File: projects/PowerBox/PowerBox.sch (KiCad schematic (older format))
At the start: 38 parts, among them CON1 USB-MICRO, CON2 USB-A-Jack, IC1 OPAMP-DUALU, P1 CONN_2, P2 CONN_2, P3 CONN_1, P4 CONN_1, P5 CONN_1, P6 CONN_1, U1 74HC595, U2 74HC595

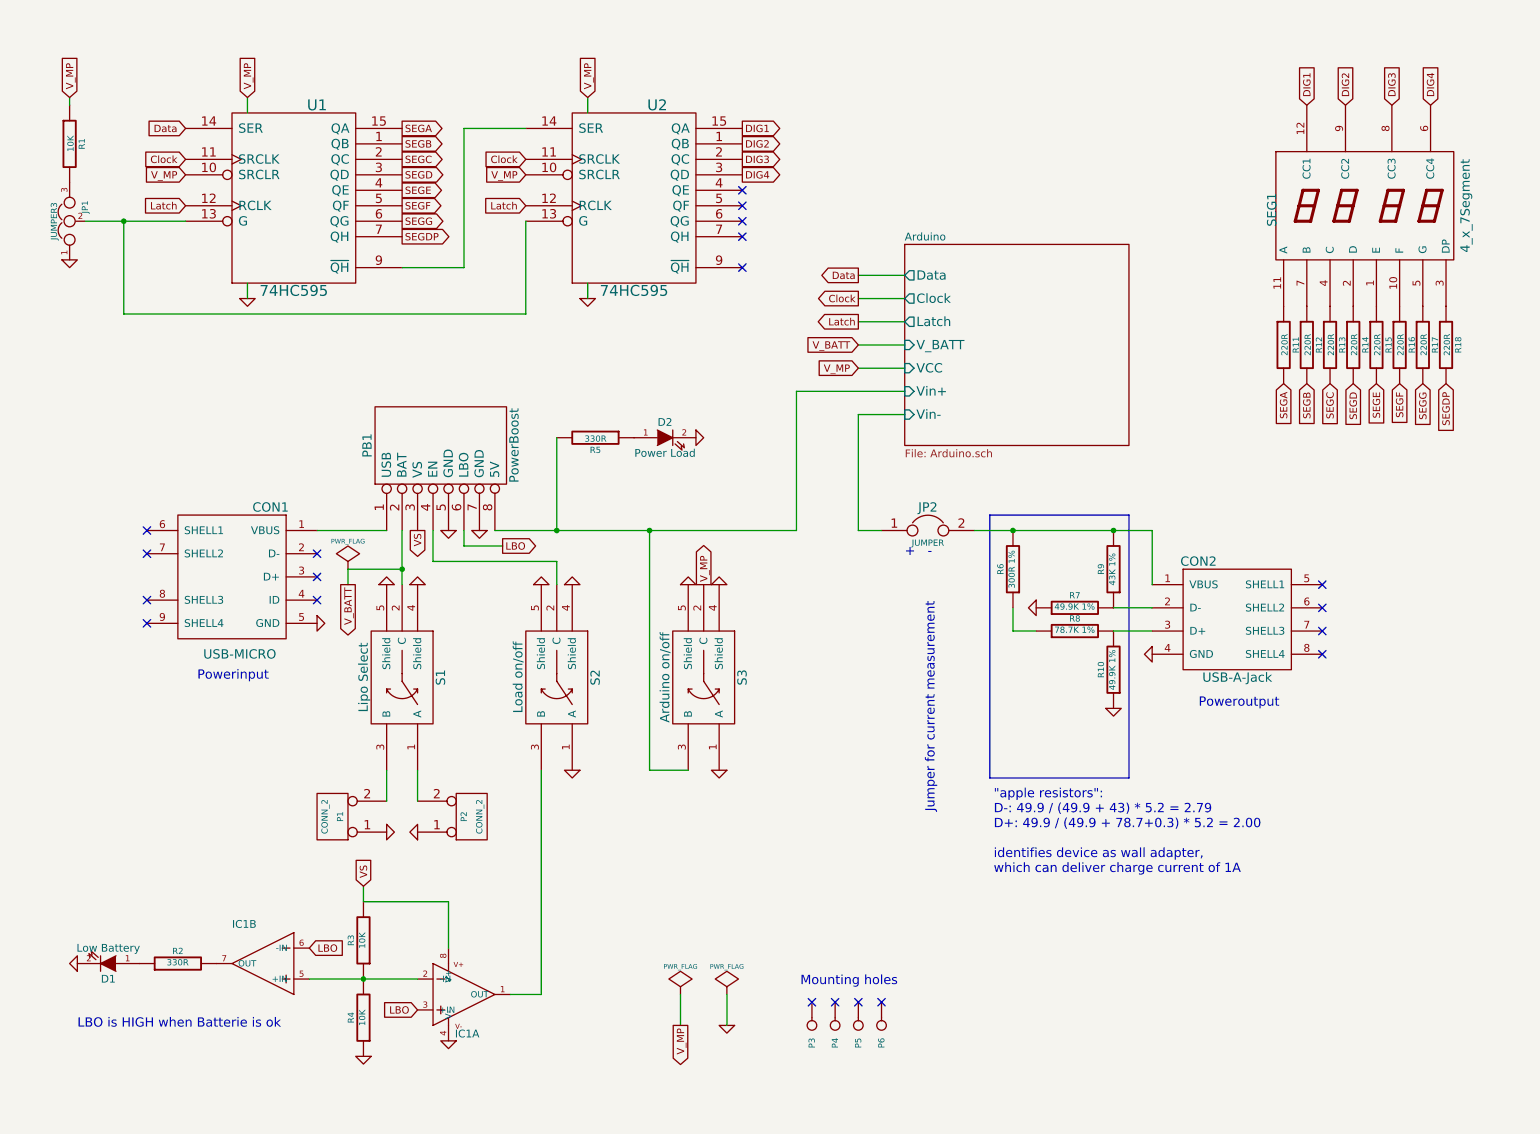
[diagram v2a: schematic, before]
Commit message: protection parts added
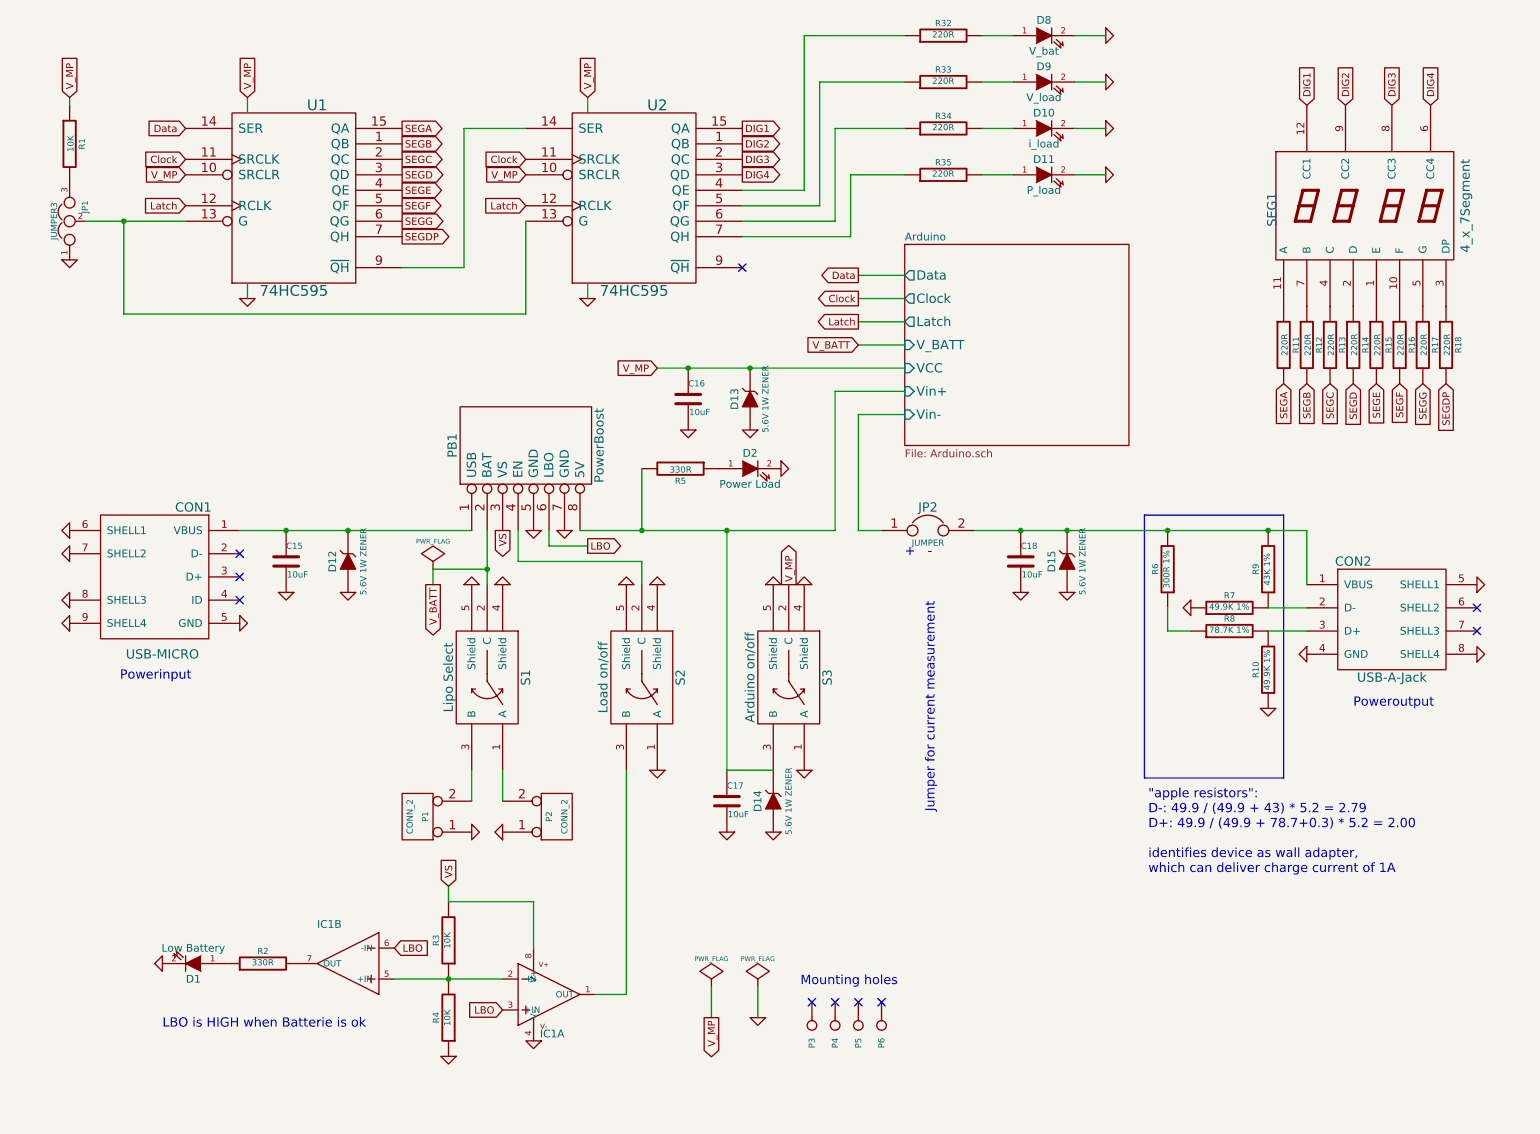
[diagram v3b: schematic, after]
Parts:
- added C15, C16, C17, C18: 10uF, frep:C0805, symbol C
- added D10: i_load, frep:LED-0805, symbol LED
- added D11: P_load, frep:LED-0805, symbol LED
- added D12, D13, D14, D15: 5.6V 1W ZENER, symbol ZENER
- added D8: V_bat, frep:LED-0805, symbol LED
- added D9: V_load, frep:LED-0805, symbol LED
- added R32, R33, R34, R35: 220R, frep:R0805, symbol R
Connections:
- net Arduino/Vin+: now also C17.1, D14.2 (K)
- net GND: now also CON1.6 (SHELL1), CON1.7 (SHELL2), CON1.8 (SHELL3), CON1.9 (SHELL4), CON2.5 (SHELL1), CON2.8 (SHELL4), C15.2, C16.2, C17.2, C18.2, D10.2 (K), D11.2 (K), D12.1 (A), D13.1 (A), D14.1 (A), D15.1 (A), D8.2 (K), D9.2 (K)
- net VCC: now also C16.1, D13.2 (K)
- net at CON1.1 (VBUS), PB1.1 (USB): now also C15.1, D12.2 (K)
- net at CON2.1 (VBUS), JP2.2, R6.2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: now also C18.1, D15.2 (K)
- net at U2.4 (QE): now also R32.1
- net at U2.5 (QF): now also R33.1
- net at U2.6 (QG): now also R34.1
- net at U2.7 (QH): now also R35.1
- new net: D11.1 (A), R35.2
- new net: D10.1 (A), R34.2
- new net: D9.1 (A), R33.2
- new net: D8.1 (A), R32.2
- no-connect marks 20 -> 10
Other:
- moved on the sheet: CON1, D1, D2, IC1A, IC1B, P1, P2, PB1, R10, R2, R3, R4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

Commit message: Switches changed
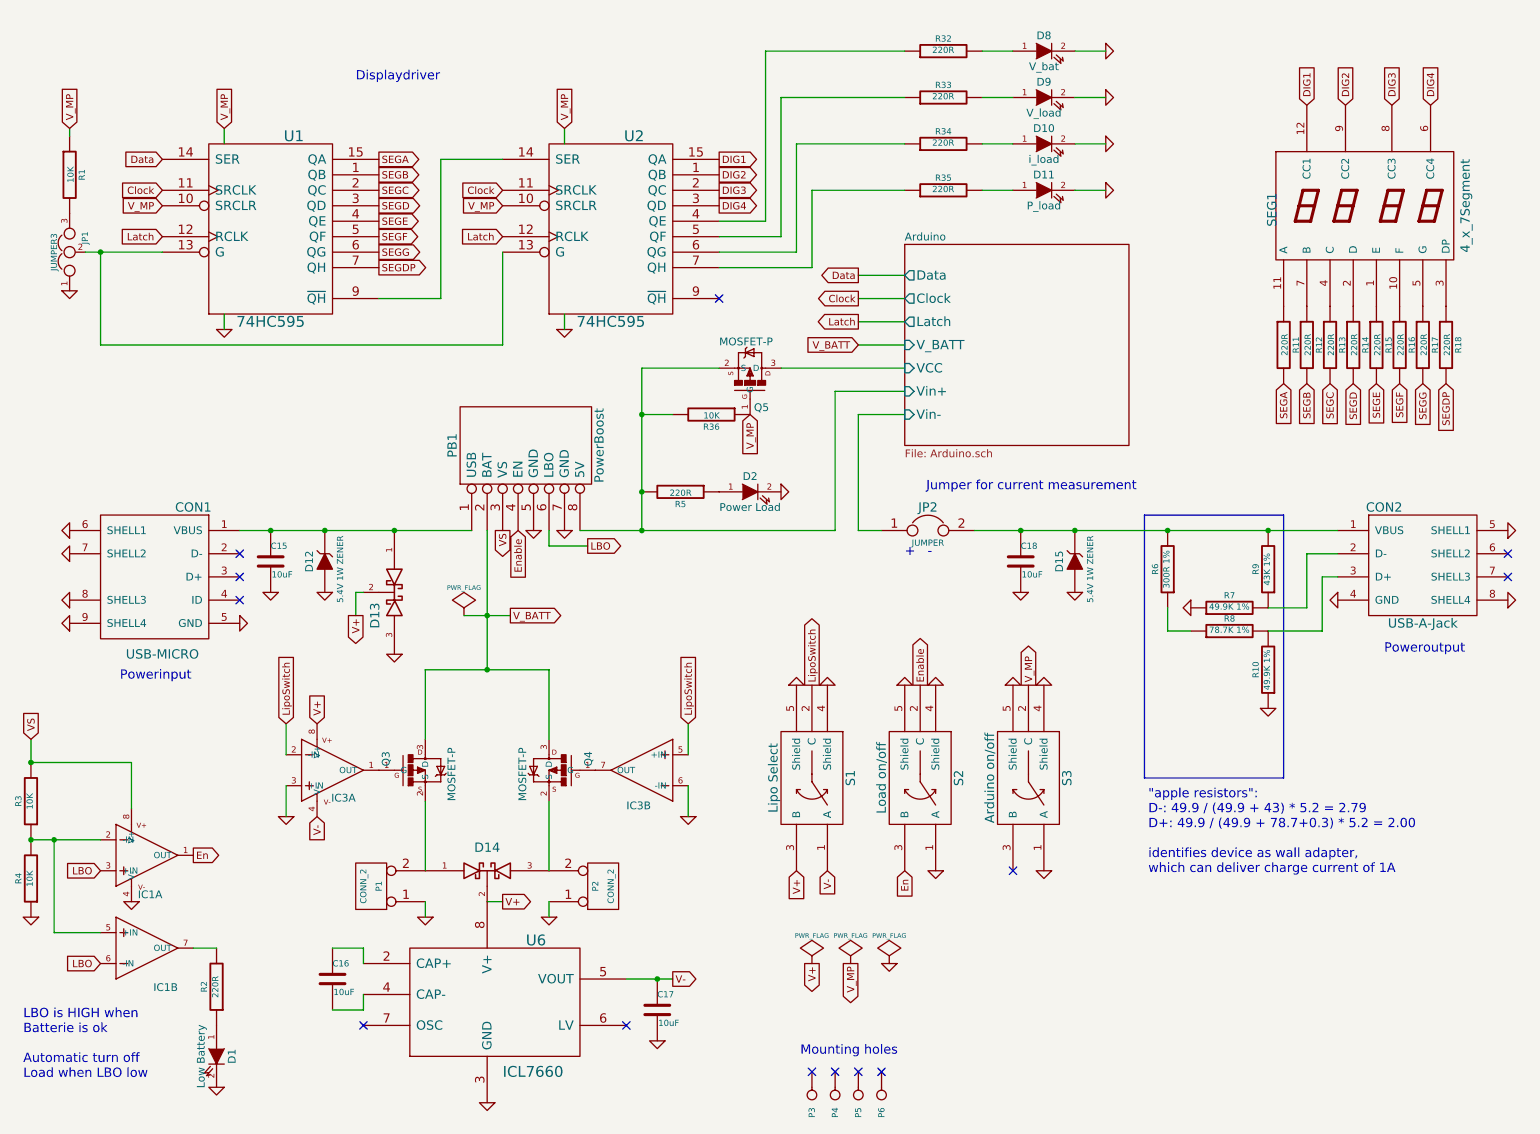
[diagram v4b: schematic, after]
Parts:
- removed D13, D14: 5.6V 1W ZENER, symbol ZENER
- added D13, D14: DOUBLE_SCH_KCOM, symbol DOUBLE_SCH_KCOM
- added IC3: OPAMP-DUALU, SparkFun-SO08, symbol OPAMP-DUALU
- added Q3, Q4, Q5: MOSFET-P, symbol MOSFET-P
- added R36: 10K, frep:R0805, symbol R
- added U6: ICL7660, symbol ICL7660
- D12, D15: value 5.6V 1W ZENER -> 5.4V 1W ZENER
- R2, R5: value 330R -> 220R
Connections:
- net Arduino/Vin+: now also Q5.2 (S), R36.2; no longer C17.1, S3.3 (B)
- net GND: now also D13.3 (cathode), IC3.3 (+IN), IC3.6 (-IN), U6.3 (GND); no longer C16.2
- net VCC: now also Q5.1 (G), R36.1; no longer C16.1
- net V_BATT: now also Q3.3 (D), Q4.3 (D); no longer S1.2 (C)
- net at C15.1, CON1.1 (VBUS), D12.2 (K)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: now also D13.1 (Anode)
- net at P2.2 (PM): now also D14.3 (cathode), Q4.2 (S); no longer S1.1 (A)
- net at P1.2 (PM): now also D14.1 (Anode), Q3.2 (S); no longer S1.3 (B)
- net Enable: now reaches PB1.4 (EN), S2.2 (C)
- net En: now reaches IC1.1 (OUT), S2.3 (B)
- new net: IC3.1 (OUT), Q3.1 (G)
- new net: IC3.7 (OUT), Q4.1 (G)
- new net: C16.1, U6.2 (CAP+)
- new net: C16.2, U6.4 (CAP-)
- new net Arduino/VCC: Q5.3 (D)
- new net LipoSwitch: IC3.2 (-IN), IC3.5 (+IN), S1.2 (C)
- new net V+: D13.2 (AK), D14.2 (AK), IC3.8 (V+), S1.3 (B), U6.8 (V+)
- new net V-: C17.1, IC3.4 (V-), S1.1 (A), U6.5 (VOUT)
- no-connect marks 10 -> 13
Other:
- note added: "Displaydriver"
- note added: "LBO is HIGH when \nBatterie is ok\n\nAutomatic turn off\nLoad when LBO low"
- note removed: "LBO is HIGH when Batterie is ok"
- moved on the sheet: C15, CON2, D1, D10, D11, D12, D15, D2, D8, D9, IC1A, IC1B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

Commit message: part informations added
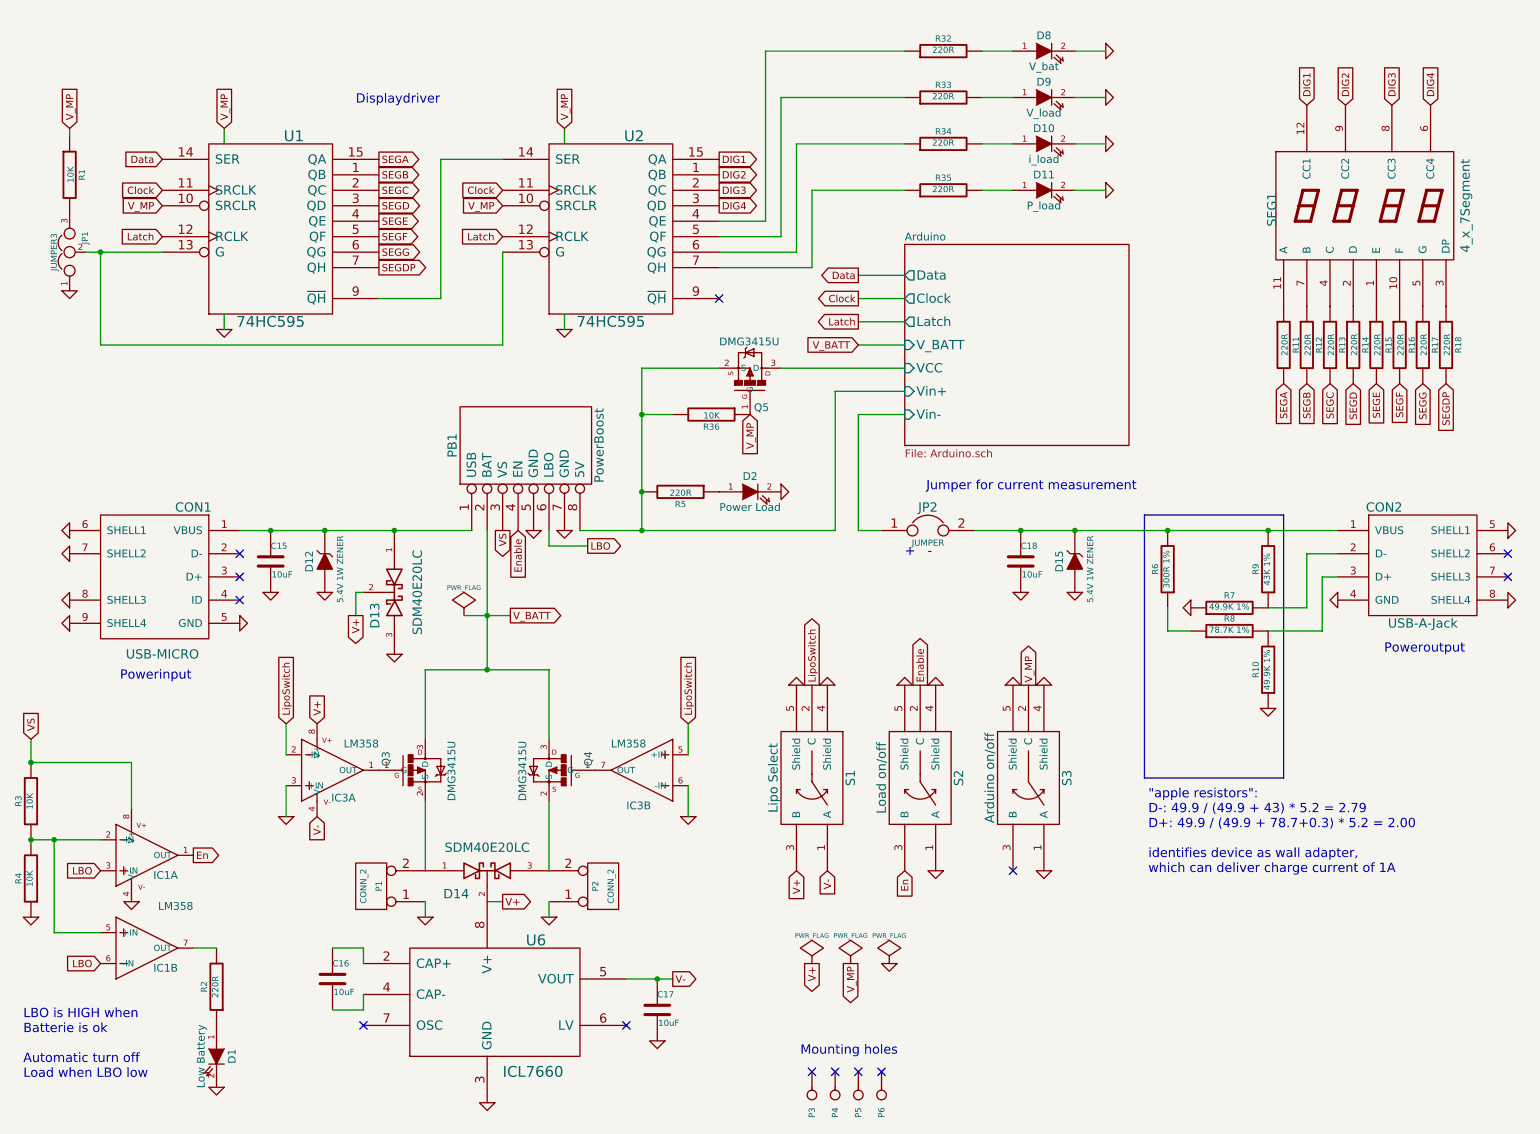
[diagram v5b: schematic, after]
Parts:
- D13, D14: value DOUBLE_SCH_KCOM -> SDM40E20LC
- IC1, IC3: value OPAMP-DUALU -> LM358
- Q3, Q4, Q5: value MOSFET-P -> DMG3415U
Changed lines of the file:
@@
 U 1 1 5583A310
 P 1600 6000
-F 0 "IC1" H 1800 5775 50  0000 R TNN
-F 1 "OPAMP-DUALU" H 1800 6200 50  0001 R TNN
+F 0 "IC1" H 1900 5900 50  0000 R TNN
+F 1 "LM358" H 1800 6200 50  0001 R TNN
 F 2 "frep:SOIC8" H 1600 6150 50  0001 C CNN
 F 3 "" H 1600 6000 60  0000 C CNN
@@
 U 2 1 5583A324
 P 1700 6600
-F 0 "IC1" H 1900 6375 50  0000 R TNN
-F 1 "OPAMP-DUALU" H 1900 6800 50  0001 R TNN
+F 0 "IC1" H 1900 6500 50  0000 R TNN
+F 1 "LM358" H 2000 6900 50  0000 R TNN
 F 2 "frep:SOIC8" H 1700 6750 50  0001 C CNN
 F 3 "" H 1700 6600 60  0000 C CNN
@@
 P 5600 2850
 F 0 "Q5" H 5625 3075 50  0000 L BNN
-F 1 "MOSFET-P" H 5400 2650 50  0000 L BNN
+F 1 "DMG3415U" H 5400 2650 50  0000 L BNN
 F 2 "" V 5750 2850 50  0001 C CNN
 F 3 "" V 5600 2850 60  0000 C CNN
@@
 P 2800 5450
 F 0 "IC3" H 3050 5300 50  0000 R TNN
-F 1 "OPAMP-DUALU" H 3000 5650 50  0001 R TNN
+F 1 "LM358" H 3200 5650 50  0000 R TNN
 F 2 "SparkFun-SO08" H 2800 5600 50  0001 C CNN
 F 3 "" H 2800 5450 60  0000 C CNN
@@
 P 4900 5450
 F 0 "IC3" H 5000 5250 50  0000 R TNN
-F 1 "OPAMP-DUALU" H 5100 5650 50  0001 R TNN
+F 1 "LM358" H 5100 5650 50  0000 R TNN
 F 2 "SparkFun-SO08" H 4900 5600 50  0001 C CNN
 F 3 "" H 4900 5450 60  0000 C CNN
@@
 P 3500 5450
 F 0 "Q3" H 3525 5675 50  0000 L BNN
-F 1 "MOSFET-P" H 3300 5250 50  0000 L BNN
+F 1 "DMG3415U" H 3300 5250 50  0000 L BNN
 F 2 "" V 3650 5450 50  0001 C CNN
 F 3 "" V 3500 5450 60  0000 C CNN
@@
 P 4300 5450
 F 0 "Q4" H 4325 5675 50  0000 L BNN
-F 1 "MOSFET-P" H 4100 5250 50  0000 L BNN
+F 1 "DMG3415U" H 4100 5250 50  0000 L BNN
 F 2 "" V 4450 5450 50  0001 C CNN
 F 3 "" V 4300 5450 60  0000 C CNN
@@
 P 3300 4300
 F 0 "D13" H 3450 4175 60  0000 C CNN
-F 1 "DOUBLE_SCH_KCOM" H 3300 4450 60  0001 C CNN
+F 1 "SDM40E20LC" H 3300 4450 60  0000 C CNN
 F 2 "" H 3300 4300 60  0000 C CNN
 F 3 "" H 3300 4300 60  0000 C CNN
@@
 U 1 1 5595799F
 P 3900 6100
-F 0 "D14" H 3900 6250 60  0000 C CNN
-F 1 "DOUBLE_SCH_KCOM" H 3900 6250 60  0001 C CNN
+F 0 "D14" H 3700 5950 60  0000 C CNN
+F 1 "SDM40E20LC" H 3900 6250 60  0000 C CNN
 F 2 "" H 3900 6100 60  0000 C CNN
 F 3 "" H 3900 6100 60  0000 C CNN
@@
 Wire Wire Line
 	5700 800  6600 800
-Text Notes 3050 1000 0    60   ~ 0
+Text Notes 3050 1150 0    60   ~ 0
 Displaydriver
 Connection ~ 3300 3900
@@
 V+
 $Comp
-L PWR_FLAG #FLG?
+L PWR_FLAG #FLG047
 U 1 1 5596ED03
 P 6000 6700
-F 0 "#FLG?" H 6000 6795 30  0001 C CNN
+F 0 "#FLG047" H 6000 6795 30  0001 C CNN
 F 1 "PWR_FLAG" H 6000 6880 30  0000 C CNN
 F 2 "" H 6000 6700 60  0000 C CNN

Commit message: netlist finished
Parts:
- removed D12, D15: 5.4V 1W ZENER, symbol ZENER
- added D10, D2: 5.3V Zener, frep:SOT23, symbol ZENER_SOT23
- D3: renamed from D13; footprint (none) -> frep:SOT23
- D4: renamed from D14; footprint (none) -> frep:SOT23
- IC2: renamed from IC3; footprint SparkFun-SO08 -> frep:SOIC8
- Q1: renamed from Q3; footprint (none) -> frep:SOT23
- Q2: renamed from Q4; footprint (none) -> frep:SOT23
- Q3: renamed from Q5; footprint (none) -> frep:SOT23
- U2: renamed from U6; footprint (none) -> frep:SOIC8
- renumbered C15 to C1, C16 to C2, C17 to C3, C18 to C4, D2 to D5, D8 to D6, D9 to D7, D10 to D8, D11 to D9, R3 to R1, R35 to R10, R6 to R11, R7 to R12, R8 to R13, R9 to R14, R10 to R15, R11 to R16, R12 to R17, R13 to R18, R14 to R19, R4 to R2, R15 to R20, R16 to R21, R17 to R22, R18 to R23, R1 to R3, R2 to R4, R36 to R6, R32 to R7, R33 to R8, R34 to R9, U2 to U3
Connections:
- net GND: now also D10.1 (A), D2.1 (A)
- net at C1.1, CON1.1 (VBUS), D3.1 (Anode)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: now also D2.3 (K)
- net at C4.1, CON2.1 (VBUS), JP2.2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: now also D10.3 (K)
- no-connect marks 13 -> 15
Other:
- note added: "Load: 5.2V, max 1A"
- moved on the sheet: C1, C4, CON1
